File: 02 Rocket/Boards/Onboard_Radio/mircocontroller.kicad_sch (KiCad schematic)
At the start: 30 parts, among them J3 USB_B_Micro, J4 SWD JST PH, U4 STM32H562RGT6, Y2 12MHz

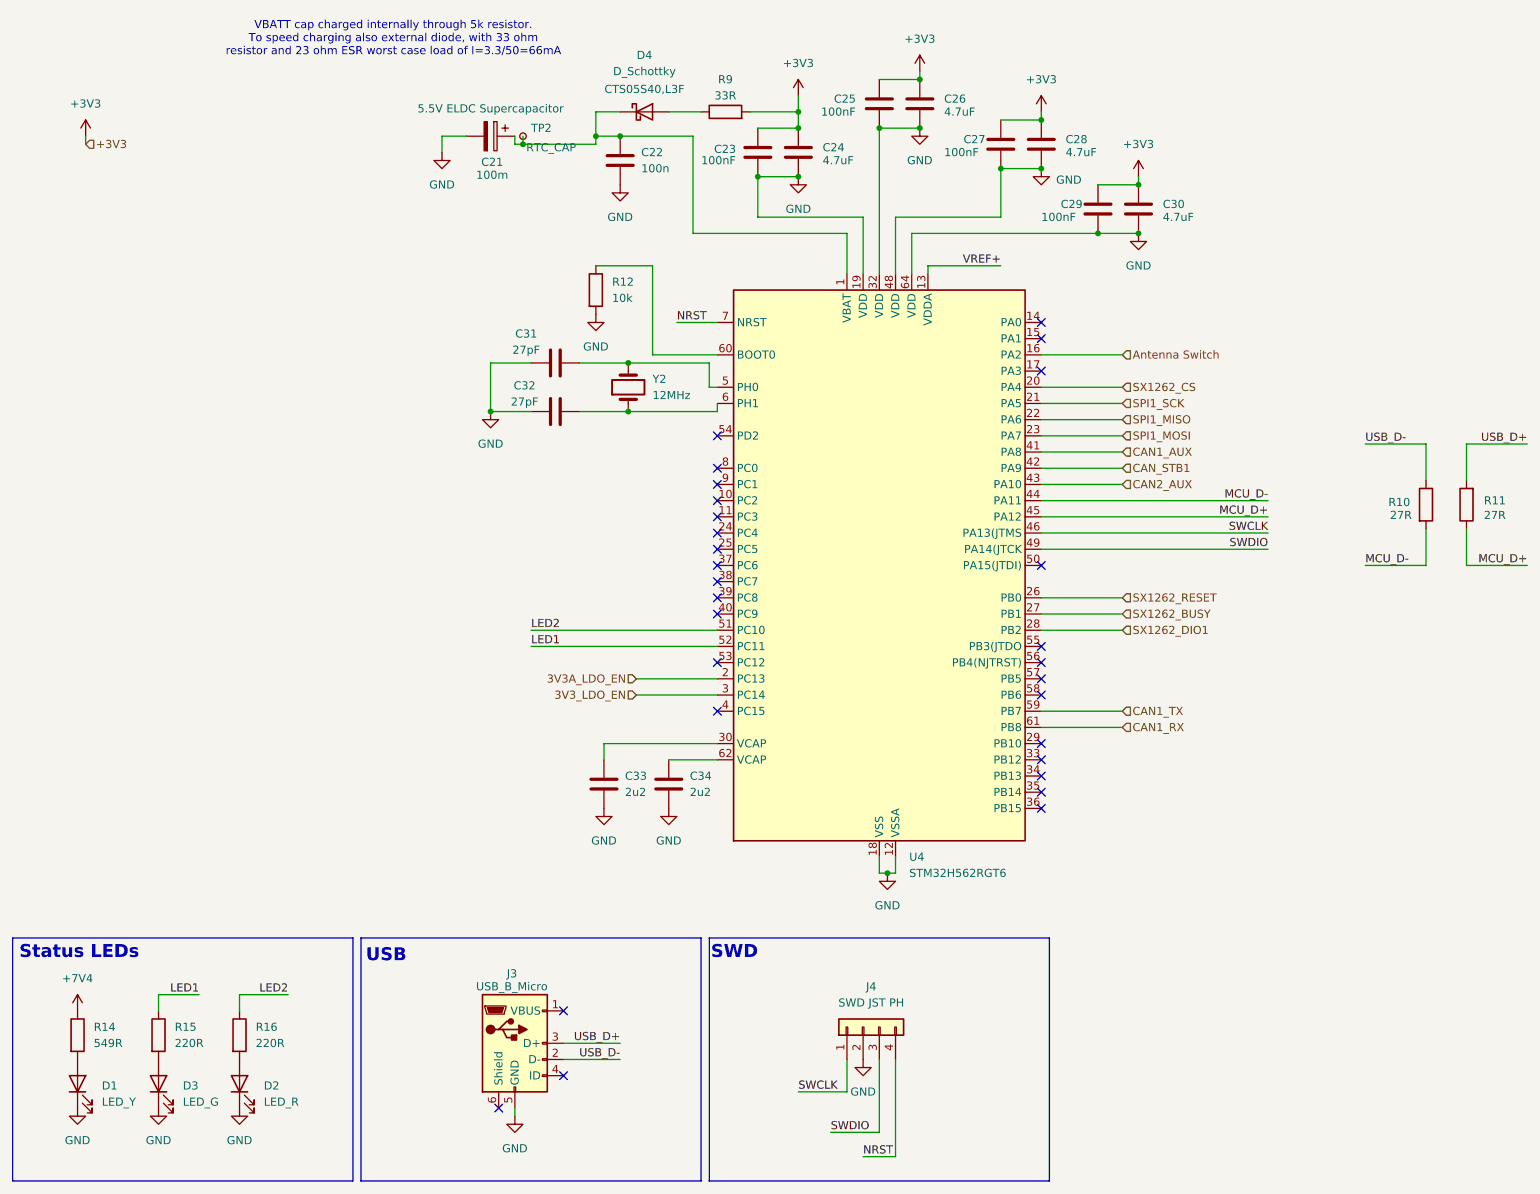
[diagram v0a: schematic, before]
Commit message: rocket, gs, jpole need review b4 order, update last of bom
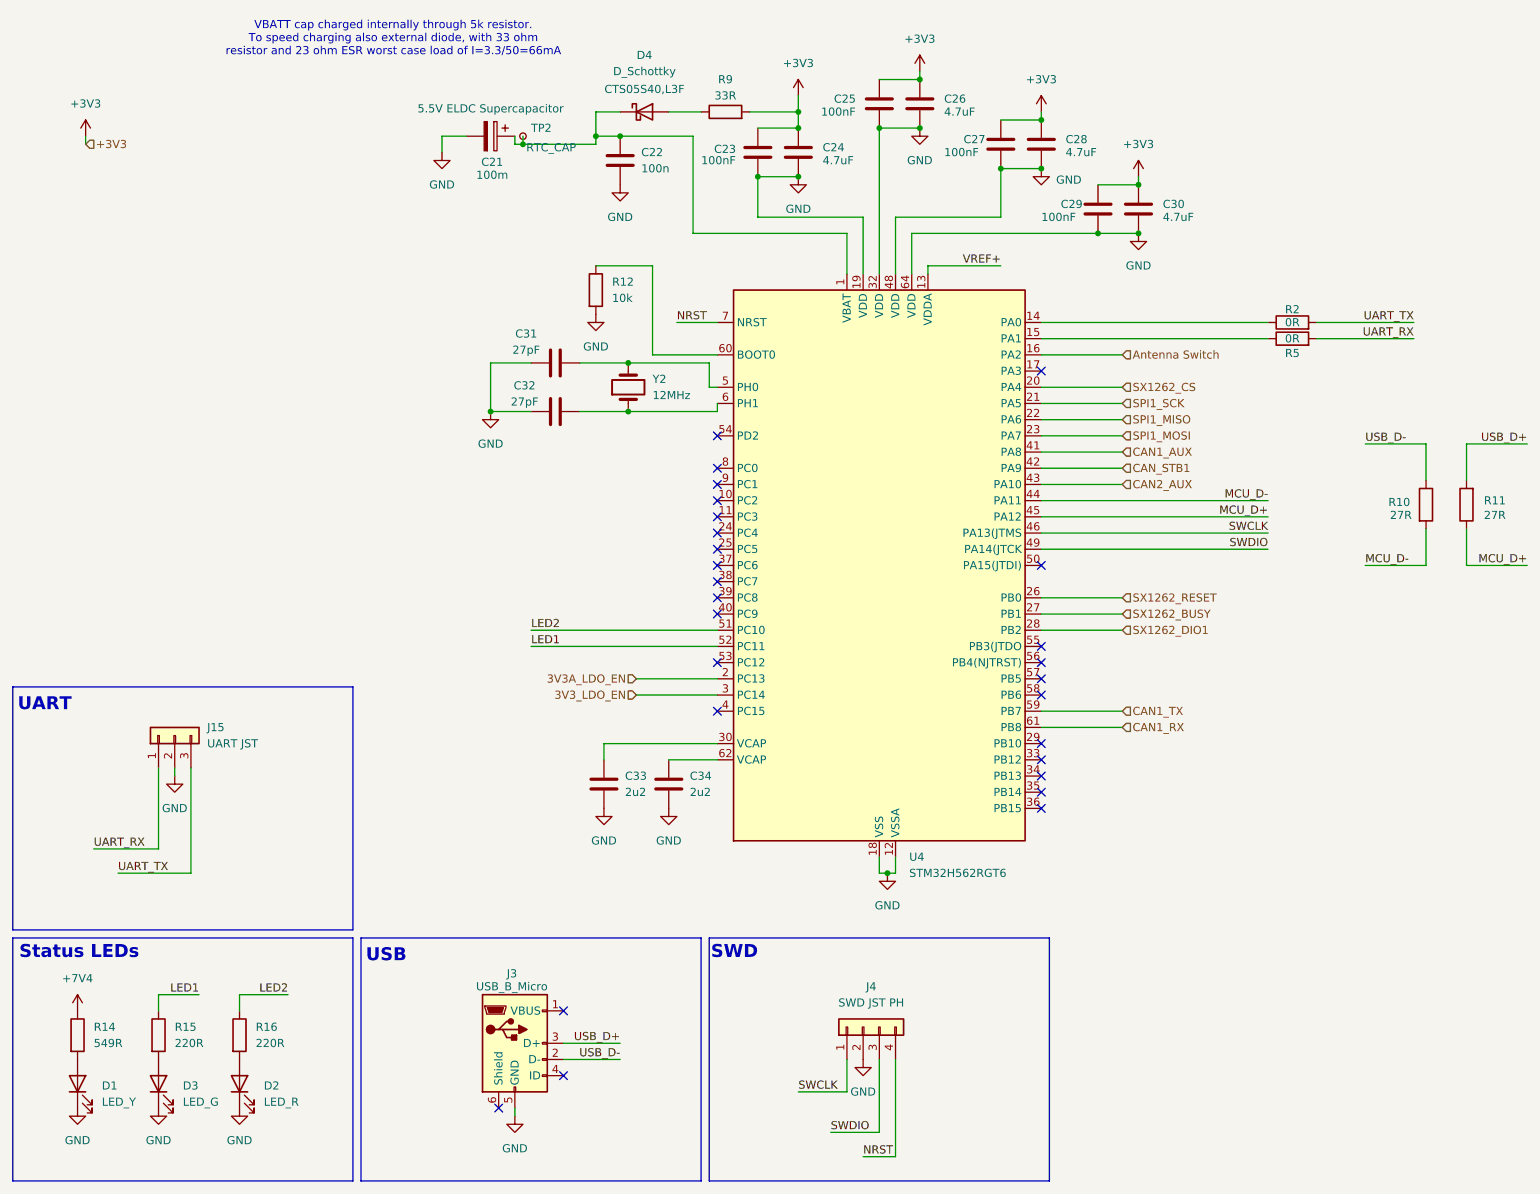
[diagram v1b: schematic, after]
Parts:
- added J15: UART JST, Connector_JST:JST_PH_B3B-PH-K_1x03_P2.00mm_Vertical, symbol Connector_Generic:Conn_01x03
- added R2, R5: 0R, Resistor_SMD:R_0402_1005Metric, symbol Device:R
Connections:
- net GND: now also J15.2 (Pin_2)
- net at U4.14 (PA0): now also R2.1
- net at U4.15 (PA1): now also R5.1
- new net UART_RX: J15.1 (Pin_1), R5.2
- new net UART_TX: J15.3 (Pin_3), R2.2
- no-connect marks 29 -> 27
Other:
- note added: "UART"

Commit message: Narottam Updates Resolved
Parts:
- removed R10, R11: 27R, Resistor_SMD:R_0603_1608Metric, symbol Device:R
- added D5: LED_Y, LED_SMD:LED_0603_1608Metric, symbol Device:LED
- added R17: 549R, Resistor_SMD:R_0603_1608Metric, symbol Device:R
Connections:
- net MCU_D+ is gone; now on net USB_D+: U4.45 (PA12)
- net MCU_D- is gone; now on net USB_D-: U4.44 (PA11)
- net +3V3: now also U4.19 (VDD), U4.32 (VDD), U4.48 (VDD), U4.64 (VDD), R17.1
- net GND: now also J3.6 (Shield), D5.1 (K); no longer U4.19 (VDD), U4.32 (VDD), U4.48 (VDD), U4.64 (VDD)
- net SWCLK: now also U4.49 (PA14(JTCK); no longer U4.46 (PA13(JTMS)
- net SWDIO: now also U4.46 (PA13(JTMS); no longer U4.49 (PA14(JTCK)
- net +7V4 renamed +5V
- new net: D5.2 (A), R17.2
- no-connect marks 27 -> 26
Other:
- moved on the sheet: C21, C23, C24, C25, C26, C27, C28, D1, D2, D3, D4, R14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

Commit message: radio board ordered!
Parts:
- R12: LCSC Part # C98220 -> RC0603FR-0710KL; Max Temp (none) -> 155; Min Temp (none) -> -55
- R2, R5: LCSC Part # (none) -> C190119; MPN (none) -> CRCW04020000Z0ED; Manufacturer (none) -> Vishay Dale; Max Temp (none) -> 155; Min Temp (none) -> -55
